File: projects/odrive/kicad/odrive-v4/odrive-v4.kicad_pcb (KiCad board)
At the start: 4 copper layers, 170 x 115 mm, 378 parts, among them J1 PC 16/2-ST, J10 ENC_M1_JST-GH, J11 ENC_SPI_JST-GH, J12 GPIO_2x4, J13 BRAKE_EXT, J2 M0 A/B/C, J3 M1 A/B/C, J4 FTSH-105-01-L-DV-K, J5 FAN 12V 150mA MAX, J6 USB4105-GF-A, J7 JST-GH-4 CAN, J8 JST-GH-4 CAN, J9 ENC_M0_JST-GH, Q1 NVMFS5C628NL | BSC027N10NS5, Q10 NVMFS5C628NL, Q11 NVMFS5C628NL, Q12 NVMFS5C628NL, Q13 NVMFS5C628NL, Q14 NVMFS5C628NL, Q15 NVMFS5C628NL, Q16 NVMFS5C628NL, Q17 NVMFS5C628NL, Q18 NVMFS5C628NL, Q19 NVMFS5C628NL, Q20 NVMFS5C628NL, Q21 NVMFS5C628NL, Q30 NVMFS5C628NL, Q31 NVMFS5C628NL, Q32 NVMFS5C628NL, Q33 NVMFS5C628NL, Q34 NVMFS5C628NL, Q35 NVMFS5C628NL, Q36 NVMFS5C628NL, Q37 NVMFS5C628NL, Q38 NVMFS5C628NL, Q39 NVMFS5C628NL, Q40 NVMFS5C628NL, Q41 NVMFS5C628NL, Q50 NVMFS5C628NL/BSC027N10NS5, Q51 NVMFS5C628NL/BSC027N10NS5, SW1 CAN_TERM, U10 TLV9062, U11 TMUX1204, U12 TLV7031, U13 TLV431, U14 74LVC1G04, U15 74LVC1G08, U16 TPD4E05U06, U2 STM32F405RGT6, U20 LM5164DDA, U21 LMR51430, U22 TLV75533PDBV, U23 TPS7A2033DBV, U25 74LVC1G06, U26 TLV7031DBV, U27 74LVC1G08, U28 TPS3840DL30, U3 DRV8353RS, U30 TPS2553DBV, U31 TPS2553DBV, U32 TPS2553DBV, U33 USBLC6-2SC6, U34 TCAN1042HGV, U35 SN74LVC2G17, U36 SN74LVC2G17, U37 SN74LVC2G17, U38 TPD4E05U06, U39 TPD4E05U06, U4 DRV8353RS, U40 SN74LVC1G125, U41 TPD4E05U06, U42 TPD1E10B06, U50 UCC27517A, U51 INA181A2, U52 TLV7031, U53 74LVC1G74, U54 74LVC1G32, U55 74LVC1G08, Y1 8MHz

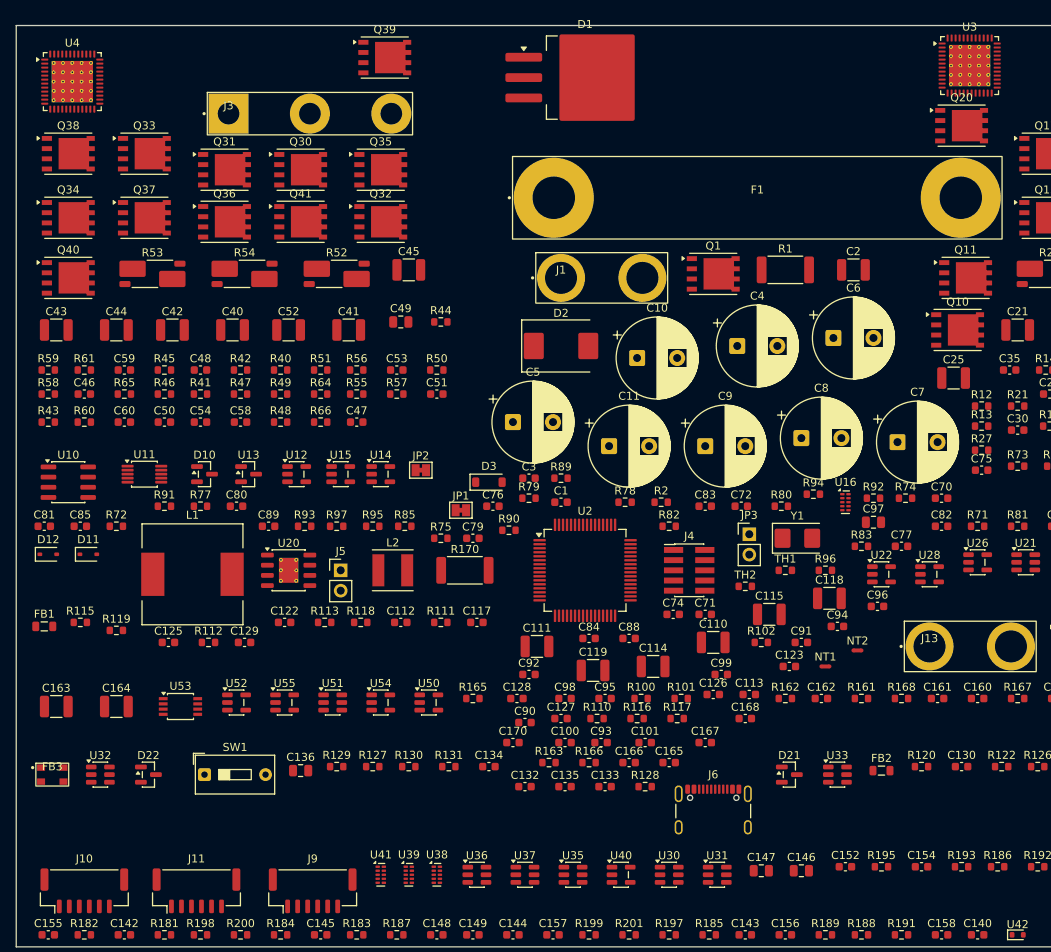
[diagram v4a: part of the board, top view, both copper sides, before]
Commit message: Mirror the two motor cells so M1 is M0's reflection
The two MotorCell sheets are structurally identical - 57 refs each, 12 FETs
each, parallel numbering (Q10-Q21 / Q30-Q41, C20-C37 / C40-C57) - so they
should be mirror images on the board: two motors that behave the same want
the same commutation geometry. Paired all 57 components 1:1 (numeric offset
plus footprint match), mirrored M0's positions about the board centre line
onto M1 (x -> 270-x, rotation negated), then re-ran the collision resolver
globally. Result: 50/57 pairs land in exact mirror symmetry, verdict still
pass with zero courtyard overlaps. This is the structural fix that matters
for the power stage; the remaining score deductions (connectors not at the
edge, decoupling distance) need human placement decisions.
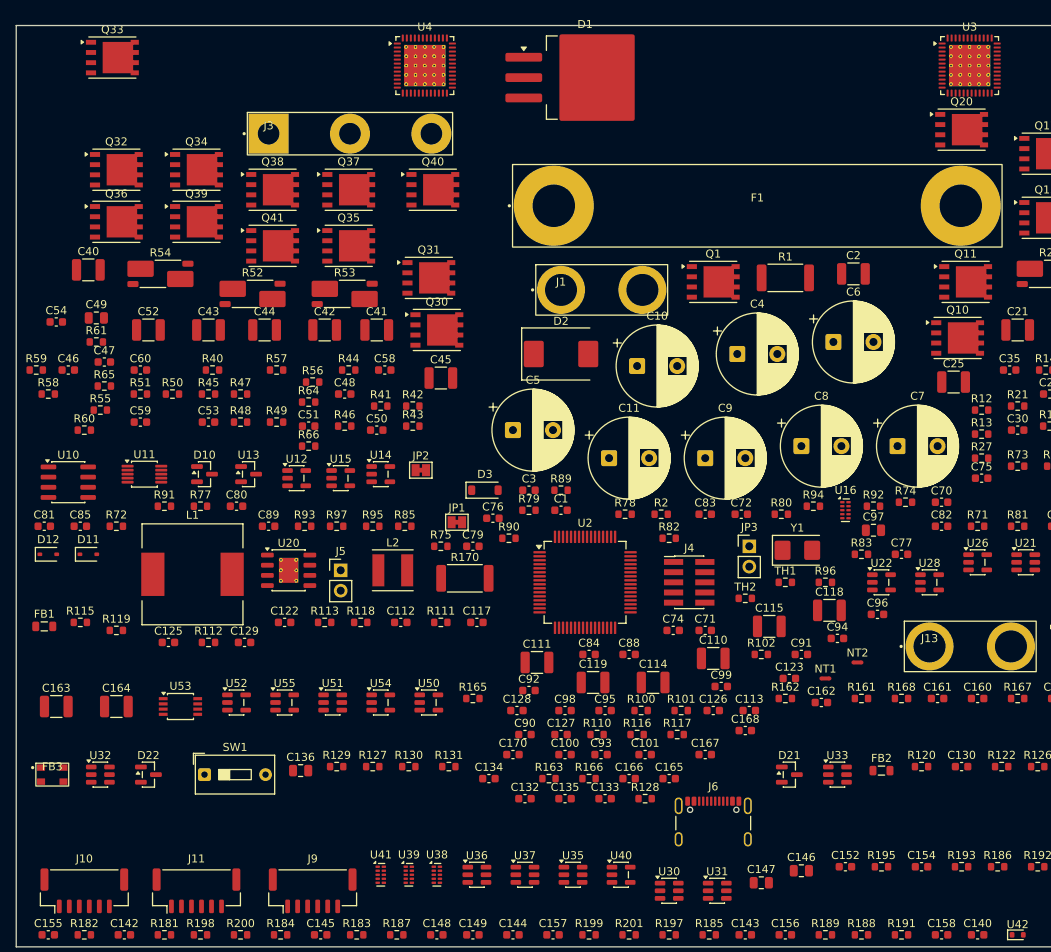
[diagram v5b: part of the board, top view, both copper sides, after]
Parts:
- moved Q40 46.8 mm to (102.0, 70.5)
- moved R43 45.5 mm to (99.5, 100.0)
- moved U4 44.0 mm to (101.0, 55.0)
- moved C49 38.0 mm to (60.0, 86.5)
- moved Q32 33.6 mm to (62.5, 68.0)
- moved R50 33.1 mm to (69.5, 96.0)
- moved C47 32.4 mm to (61.0, 92.0)
- moved R55 32.1 mm to (60.5, 98.0)
- moved Q39 31.2 mm to (72.5, 74.5)
- moved Q31 28.9 mm to (101.5, 81.5)
- moved C50 26.5 mm to (95.0, 100.5)
- moved Q30 26.2 mm to (102.5, 88.0)
- moved Q38 25.9 mm to (82.0, 70.5)
- moved Q37 25.7 mm to (91.5, 70.5)
- moved C53 24.4 mm to (74.0, 99.5)
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
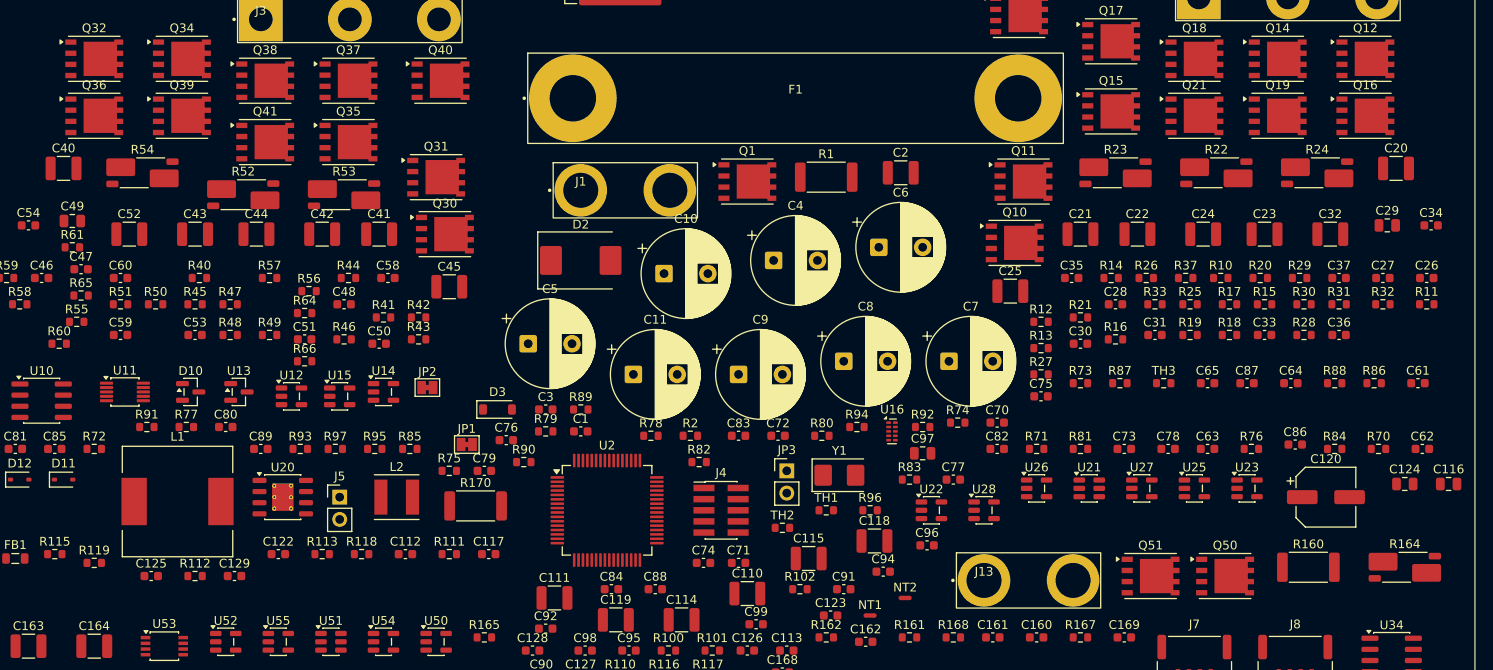
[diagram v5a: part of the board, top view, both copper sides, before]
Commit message: Line up the bulk electrolytic bank
C4-C11 were scattered across 14mm of vertical spread from the shelf packing;
they are one bank on one net and should sit in a row like the ODrive
reference, both to look right and to give the DCBUS routing a straight run.
Snapped them to an even pitch on a single line, then re-ran the collision
resolver, which nudged a few back by up to 2.5mm to stay legal - close enough
to read as a row. Board stays at verdict pass with zero courtyard overlaps.
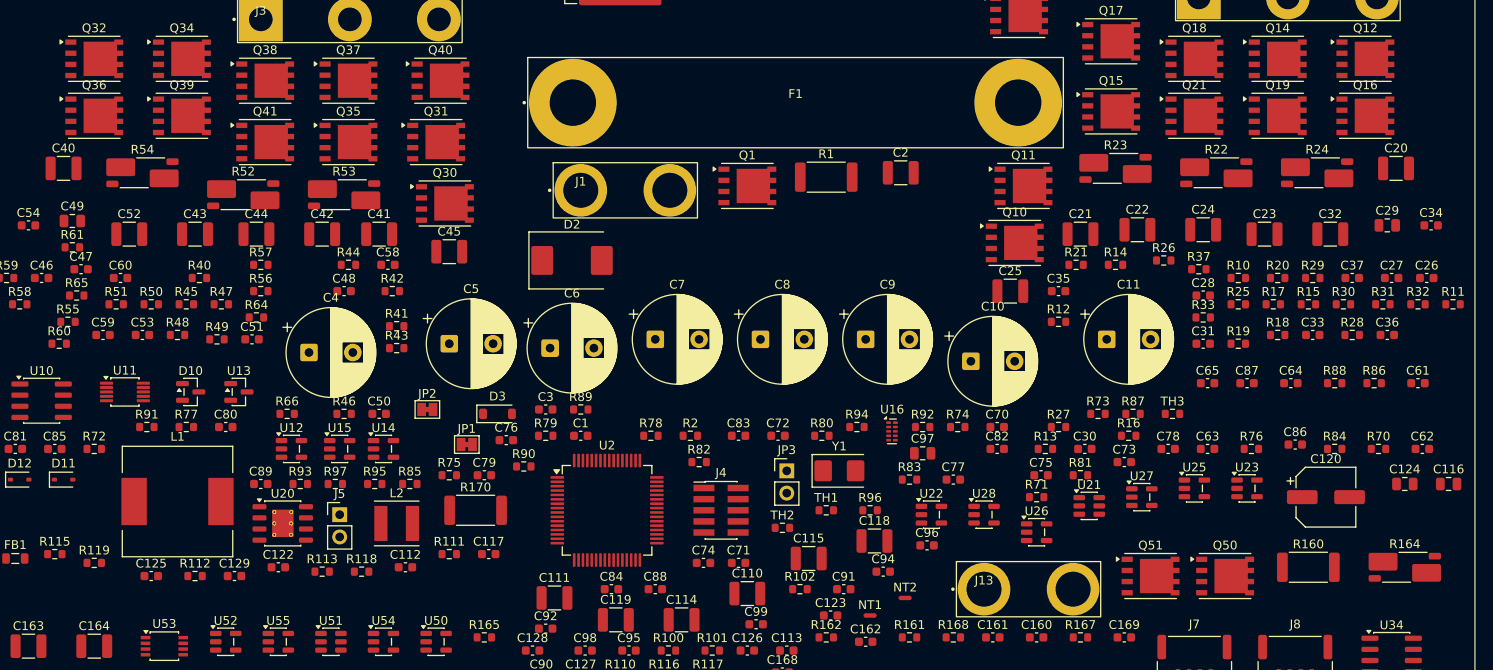
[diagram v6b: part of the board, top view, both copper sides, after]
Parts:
- moved C11 54.1 mm to (178.0, 100.0)
- moved C4 54.0 mm to (87.0, 101.5)
- moved C6 39.2 mm to (114.5, 101.0)
- moved C10 36.4 mm to (162.5, 102.5)
- moved C7 33.6 mm to (126.5, 100.0)
- moved C9 15.0 mm to (150.5, 100.0)
- moved C30 12.0 mm to (175.5, 112.5)
- moved R13 11.5 mm to (171.0, 112.5)
- moved R16 11.1 mm to (180.5, 111.0)
- moved C28 10.0 mm to (189.0, 95.0)
- moved C8 9.82 mm to (138.5, 100.0)
- moved C5 9.00 mm to (103.0, 100.5)
- moved C75 9.00 mm to (170.5, 115.5)
- moved R46 8.50 mm to (91.0, 108.5)
- moved C50 8.00 mm to (95.0, 108.5)
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
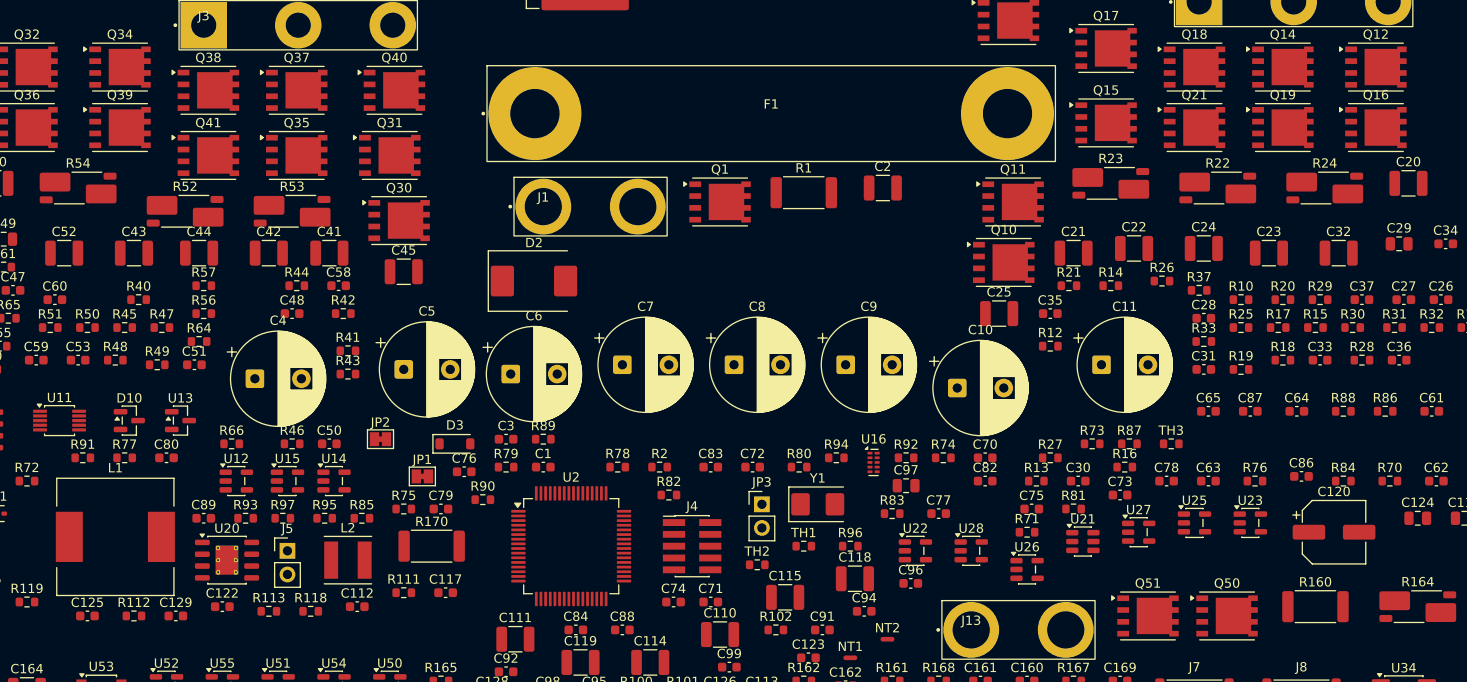
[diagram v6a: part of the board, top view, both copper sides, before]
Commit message: Pin the electrolytic bank to one line, resolve around it
The previous alignment pass put C4-C11 on a row and then let the collision
resolver push them back off it by up to 2.5mm. Fixed by pinning the eight bank
caps during resolution: they hold the exact row (y=100.0 for all eight, even
pitch) and everything else moves out of the way instead. Board back to verdict
pass with zero courtyard overlaps.
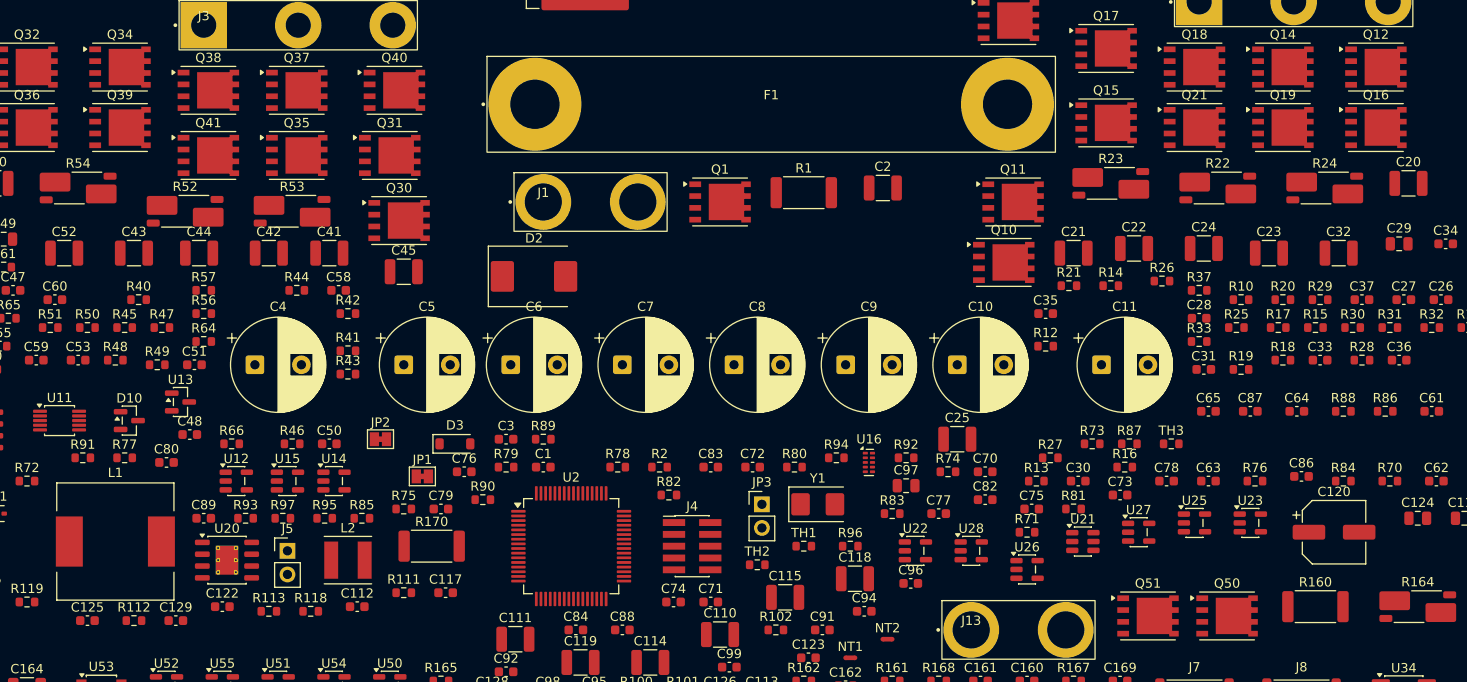
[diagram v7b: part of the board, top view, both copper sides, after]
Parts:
- moved C48 17.0 mm to (80.0, 107.5)
- moved C25 14.2 mm to (162.5, 108.0)
- moved C10 2.50 mm to (162.5, 100.0)
- moved C82 2.00 mm to (165.5, 114.5)
- moved U13 2.00 mm to (79.0, 104.0)
- moved R74 1.58 mm to (161.5, 111.5)
- moved C4 1.50 mm to (87.0, 100.0)
- moved C70 1.50 mm to (165.5, 111.5)
- moved C6 1.00 mm to (114.5, 100.0)
- moved F1 1.00 mm to (142.5, 72.0)
- moved C125 0.50 mm to (69.0, 127.5)
- moved C129 0.50 mm to (78.5, 127.5)
- moved C28 0.50 mm to (188.5, 95.0)
- moved C35 0.50 mm to (172.0, 94.5)
- moved C5 0.50 mm to (103.0, 100.0)
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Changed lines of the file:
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@@
 	(footprint "Resistor_SMD:R_0603_1608Metric"
 		(layer "F.Cu")
-		(at 91.5 91.5)
+		(at 91.5 92)
 		(property "Reference" "R44"
 			(at 0 -1.43)
@@
 	(footprint "Resistor_SMD:R_0603_1608Metric"
 		(layer "F.Cu")
-		(at 145.5 111)
+		(at 145 111)
 		(property "Reference" "R80"
 			(at 0 -1.43)
@@
 	(footprint "Capacitor_THT:CP_Radial_D10.0mm_P5.00mm"
 		(layer "F.Cu")
-		(at 162.5 102.5)
+		(at 162.5 100)
 		(property "Reference" "C10"
 			(at 2.5 -6.25)
@@
 	(footprint "Resistor_SMD:R_0603_1608Metric"
 		(layer "F.Cu")
-		(at 172.5 98)
+		(at 172 98)
 		(property "Reference" "R12"
 			(at 0 -1.43)
@@
 	(footprint "Capacitor_SMD:C_0603_1608Metric"
 		(layer "F.Cu")
-		(at 172.5 94.5)
+		(at 172 94.5)
 		(property "Reference" "C35"
 			(at 0 -1.43)
@@
 	(footprint "Resistor_SMD:R_0603_1608Metric"
 		(layer "F.Cu")
-		(at 161 110)
+		(at 161.5 111.5)
 		(property "Reference" "R74"
 			(at 0 -1.43)
@@
 	(footprint "Capacitor_SMD:C_0603_1608Metric"
 		(layer "F.Cu")
-		(at 165.5 110)
+		(at 165.5 111.5)
 		(property "Reference" "C70"
 			(at 0 -1.43)
@@
 	(footprint "Capacitor_THT:CP_Radial_D10.0mm_P5.00mm"
 		(layer "F.Cu")
-		(at 87 101.5)
+		(at 87 100)
 		(property "Reference" "C4"
 			(at 2.5 -6.25)
@@
 	(footprint "Package_SON:USON-10_2.5x1.0mm_P0.5mm"
 		(layer "F.Cu")
-		(at 153.5 110.5)
+		(at 153 110.5)
 		(property "Reference" "U16"
 			(at 0.01829 -2.5)
@@
 	(footprint "Capacitor_SMD:C_1210_3225Metric"
 		(layer "F.Cu")
-		(at 167 94.5)
+		(at 162.5 108)
 		(property "Reference" "C25"
 			(at 0 -2.3)
@@
 	(footprint "Package_TO_SOT_SMD:SOT-23"
 		(layer "F.Cu")
-		(at 79 106)
+		(at 79 104)
 		(property "Reference" "U13"
 			(at 0 -2.4)
@@
 	(footprint "Capacitor_SMD:C_0603_1608Metric"
 		(layer "F.Cu")
-		(at 91 94.5)
+		(at 80 107.5)
 		(property "Reference" "C48"
 			(at 0 -1.43)
@@
 	(footprint "Resistor_SMD:R_0603_1608Metric"
 		(layer "F.Cu")
-		(at 96.5 94.5)
+		(at 97 94.5)
 		(property "Reference" "R42"
 			(at 0 -1.43)
@@
 	(footprint "Capacitor_SMD:C_0603_1608Metric"
 		(layer "F.Cu")
-		(at 69 127)
+		(at 69 127.5)
 		(property "Reference" "C125"
 			(at 0 -1.43)
@@
 	(footprint "Resistor_SMD:R_0603_1608Metric"
 		(layer "F.Cu")
-		(at 74 127)
+		(at 74 127.5)
 		(property "Reference" "R112"
 			(at 0 -1.43)
@@
 	(footprint "Capacitor_SMD:C_0603_1608Metric"
 		(layer "F.Cu")
-		(at 189 95)
+		(at 188.5 95)
 		(property "Reference" "C28"
 			(at 0 -1.43)
@@
 	(footprint "Resistor_SMD:R_0603_1608Metric"
 		(layer "F.Cu")
-		(at 189 97.5)
+		(at 188.5 97.5)
 		(property "Reference" "R33"
 			(at 0 -1.43)
@@
 	(footprint "Capacitor_THT:CP_Radial_D10.0mm_P5.00mm"
 		(layer "F.Cu")
-		(at 114.5 101)
+		(at 114.5 100)
 		(property "Reference" "C6"
 			(at 2.5 -6.25)
@@
 	(footprint "Capacitor_SMD:C_0603_1608Metric"
 		(layer "F.Cu")
-		(at 78.5 127)
+		(at 78.5 127.5)
 		(property "Reference" "C129"
 			(at 0 -1.43)
@@
 	(footprint "Resistor_SMD:R_0603_1608Metric"
 		(layer "F.Cu")
-		(at 193 96)
+		(at 192.5 96)
 		(property "Reference" "R25"
 			(at 0 -1.43)
@@
 	(footprint "Capacitor_THT:CP_Radial_D10.0mm_P5.00mm"
 		(layer "F.Cu")
-		(at 103 100.5)
+		(at 103 100)
 		(property "Reference" "C5"
 			(at 2.5 -6.25)
@@
 	(footprint "Inductor_SMD:L_12x12mm_H8mm"
 		(layer "F.Cu")
-		(at 72 118.5)
+		(at 72 119)
 		(property "Reference" "L1"
 			(at 0 -7.4)
@@
 	(footprint "Capacitor_SMD:C_0603_1608Metric"
 		(layer "F.Cu")
-		(at 77.5 110)
+		(at 77.5 110.5)
 		(property "Reference" "C80"
 			(at 0 -1.43)
@@
 	(footprint "Resistor_SMD:R_0603_1608Metric"
 		(layer "F.Cu")
-		(at 81 97.5)
+		(at 81.5 97.5)
 		(property "Reference" "R64"
 			(at 0 -1.43)
@@
 	(footprint "odrive_footprints:TerminalBlock_Phoenix_PC-16-2-ST-10.16mm"
 		(layer "F.Cu")
-		(at 118 83)
+		(at 118 82.5)
 		(property "Reference" "J1"
 			(at 0 -1)
@@
 	(footprint "Resistor_SMD:R_0603_1608Metric"
 		(layer "F.Cu")
-		(at 81.5 91.5)
+		(at 81.5 92)
 		(property "Reference" "R57"
 			(at 0 -1.43)
@@
 	(footprint "Resistor_SMD:R_0603_1608Metric"
 		(layer "F.Cu")
-		(at 209.5 96)
+		(at 209 96)
 		(property "Reference" "R31"
 			(at 0 -1.43)
@@
 	(footprint "odrive_footprints:Fuse_Littelfuse_MEGA_BoltDown"
 		(layer "F.Cu")
-		(at 142.5 73)
+		(at 142.5 72)
 		(property "Reference" "F1"
 			(at 0 -1)
@@
 	(footprint "Diode_SMD:D_SMC"
 		(layer "F.Cu")
-		(at 117 91)
+		(at 117 90.5)
 		(property "Reference" "D2"
 			(at 0 -4.1)
@@
 	(footprint "Capacitor_SMD:C_0603_1608Metric"
 		(layer "F.Cu")
-		(at 165.5 112.5)
+		(at 165.5 114.5)
 		(property "Reference" "C82"
 			(at 0 -1.43)
@@
 	(footprint "Capacitor_SMD:C_0603_1608Metric"
 		(layer "F.Cu")
-		(at 96 91.5)
+		(at 96 92)
 		(property "Reference" "C58"
 			(at 0 -1.43)
